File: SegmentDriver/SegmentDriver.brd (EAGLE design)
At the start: 175 x 175 mm, 221 parts, among them IC1 ATMEGA644A, IC2 PCA9555PW, IC3 4511D, K1 691313710002, K10 M02-MOLEX-104188-0210, K11 M02-MOLEX-104188-0210, K12 M02-MOLEX-104188-0210, K13 M02-MOLEX-104188-0210, K14 M02-MOLEX-104188-0210, K15 M02-MOLEX-104188-0210, K16 M02-MOLEX-104188-0210, K17 691210910004, K18 691210910004, K19 691210910004, K2 691313710002, K20 691210910004, K21 691210910004, K22 691210910004, K23 691210910004, K24 691210910004, K25 691210910004, K3 691322310002, K4 691322310002, K6 61200621621, K7 61201021621, K8 M02-MOLEX-104188-0210, K9 M02-MOLEX-104188-0210, Q1 MOSFET-NCHANNEL-FDMS5672, Q2 MOSFET-NCHANNEL-FDMS5672, Q3 MOSFET-NCHANNEL-FDMS5672, Q4 MOSFET-NCHANNEL-FDMS5672, Q5 MOSFET-NCHANNEL-FDMS5672, Q6 MOSFET-NCHANNEL-FDMS5672, Q7 MOSFET-NCHANNEL-FDMS5672, Q8 MOSFET-NCHANNEL-FDMS5672, Q9 MOSFET-NCHANNEL-FDMS5672, SW1 SPST_TACT-EVQQ2, U1 DS1307SO8-TIGHT, U10 FOD8321, U11 FOD8321, U15 DMP2215L-7, U16 DMP2215L-7, U3 FOD8321, U4 FOD8321, U5 FOD8321, U6 FOD8321, U7 FOD8321, U8 FOD8321, U9 FOD8321, X1 53261-03, X2 53261-03, X3 53261-03, X4 53261-03, X5 53261-03, X6 53261-03, Y2 32.768kHz

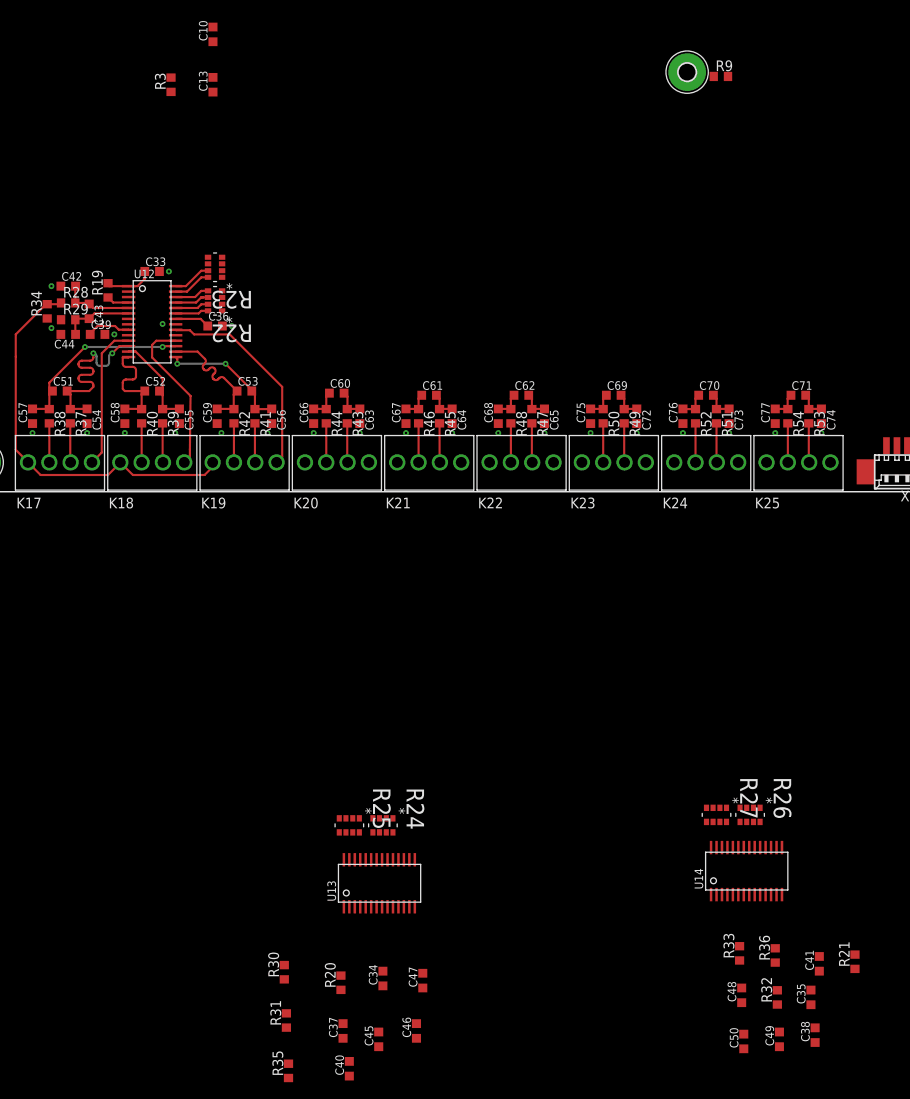
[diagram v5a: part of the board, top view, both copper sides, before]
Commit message: RTD AD layout, brd and sch remade consistent
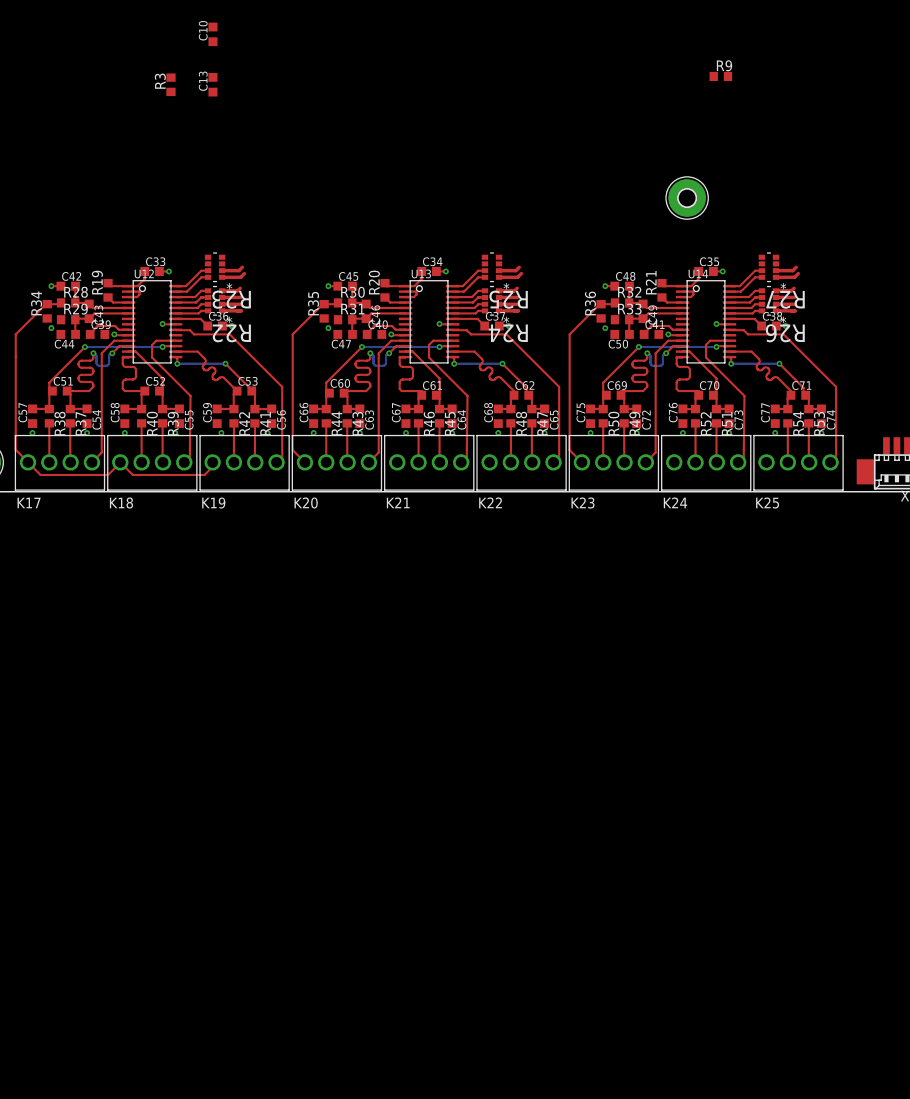
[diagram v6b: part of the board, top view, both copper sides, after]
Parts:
- moved R35 90.6 mm to (44.2, 21.5)
- moved C45 89.8 mm to (46.8, 24.5), turned to 0 degrees
- moved C49 88.3 mm to (82.2, 21.5), turned to 270 degrees
- moved C40 87.6 mm to (50.2, 18.8), turned to 0 degrees
- moved C35 87.4 mm to (89.8, 26.2), turned to 0 degrees
- moved C46 86.0 mm to (49.2, 21.5), turned to 270 degrees
- moved C37 85.9 mm to (64.2, 19.8), turned to 0 degrees
- moved C48 85.7 mm to (79.8, 24.5), turned to 0 degrees
- moved C50 85.5 mm to (79.8, 18.8), turned to 180 degrees
- moved R32 84.8 mm to (79.8, 22.5), turned to 0 degrees
- moved C38 84.7 mm to (97.2, 19.8), turned to 0 degrees
- moved C34 84.4 mm to (56.8, 26.2), turned to 0 degrees
- moved R31 83.8 mm to (46.8, 20.5), turned to 0 degrees
- moved R21 83.2 mm to (84.5, 24.0)
- moved R20 82.7 mm to (51.5, 24.0)
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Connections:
- net AD1_!CS renamed !CS!_AD1
- net AD1_!DRDY renamed !DRDY!_AD1
- net AD1_!RESET renamed !RESET!_AD1
- net AD1_BIASP renamed BIASP_AD1
- net AD1_IEXC1 renamed IEXC1_AD1
- net AD1_REFN0 renamed REFN0_AD1
- net AD1_REFP0 renamed REFP0_AD1
- net AD1_START renamed START_AD1
- net AD2_!CS renamed !CS!_AD2
- net AD2_!DRDY renamed !DRDY!_AD2
- net AD2_!RESET renamed !RESET!_AD2
- net AD2_IEXC1 renamed IEXC1_AD2
- net AD2_REFN0 renamed REFN0_AD2
- net AD2_REFP0 renamed REFP0_AD2
- net AD2_START renamed START_AD2
- net AD3_!CS renamed !CS!_AD3
- net AD3_!DRDY renamed !DRDY!_AD3
- net AD3_!RESET renamed !RESET!_AD3
- net AD3_IEXC1 renamed IEXC1_AD3
- net AD3_REFN0 renamed REFN0_AD3
- net AD3_REFP0 renamed REFP0_AD3
- net AD3_START renamed START_AD3
- net N$30 renamed 9_AD1
- net N$41 renamed 9_AD2
- net N$53 renamed 9_AD3
- net N$54 renamed 28_AD1
- net N$55 renamed 27_AD1
- net N$56 renamed 26_AD1
- net N$57 renamed 25_AD1
- net N$58 renamed 24_AD1
- net N$59 renamed 23_AD1
- net N$65 renamed 23_AD2
- net N$66 renamed 25_AD2
- net N$67 renamed 24_AD2
- net N$68 renamed 27_AD2
- net N$69 renamed 26_AD2
- net N$70 renamed 28_AD2
- net N$71 renamed 23_AD3
- net N$72 renamed 25_AD3
- net N$73 renamed 24_AD3
- net N$74 renamed 27_AD3
- net N$75 renamed 26_AD3
- net N$76 renamed 28_AD3
- removed net AD2_BIASP: K20.1, K21.1, K22.1, R30.1, R32.1, R35.2, R36.2
- removed net AD3_BIASP: K23.1, K24.1, K25.1
- new net BIASP_AD2: K20.1, K21.1, K22.1, R30.1, R35.2
- new net BIASP_AD3: K23.1, K24.1, K25.1, R32.1, R36.2
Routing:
- net GND: track 29.2 -> 58.8 mm, vias 8 -> 20
- net IEXC1_AD3: track 0.00 -> 24.8 mm
- net IEXC1_AD2: track 0.00 -> 24.8 mm
- net BIASP_AD3: track 0.00 -> 22.8 mm
- net BIASP_AD2: track 0.00 -> 22.8 mm
- net AD3_AIN1: track 3.32 -> 23.1 mm, vias 0 -> 2
- net AD2_AIN1: track 3.55 -> 23.1 mm, vias 0 -> 2
- net AD3_AIN3: track 0.00 -> 19.2 mm
- net AD2_AIN3: track 0.00 -> 19.2 mm
- net AD3_AIN2: track 3.32 -> 22.0 mm, vias 0 -> 2
- net AD2_AIN2: track 3.57 -> 22.0 mm, vias 0 -> 2
- net AD3_AIN0: track 0.00 -> 17.3 mm
- net AD2_AIN0: track 0.00 -> 17.3 mm
- net AD2_AIN7: track 3.32 -> 15.2 mm
- net AD3_AIN7: track 3.30 -> 15.2 mm
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
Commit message: added power rails
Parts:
- removed SW1: SPST_TACT-EVQQ2, adafruit:EVQ-Q2
- added C81, C84: 4.7uF, rcl:C0603K
- added C82, C83, C85: 4.7uF, rcl:C0805K
- added R62, R63, R64, R65, R66, R67, R68, R69, R70: 100k, rcl:R0603
- added SW2: (no value), simbits:434153017835
- added U18: 7808, simbits:D2PACK/A
- added U19: ADP3333ARM-5, simbits:MSOP-8
- added U20: 7805, simbits:D2PACK/A
- moved C10 204.4 mm to (235.0, 42.5)
- moved C11 204.4 mm to (235.0, 48.5)
- moved C12 204.4 mm to (235.0, 53.5)
- moved C13 204.4 mm to (235.0, 36.5)
- moved C6 204.4 mm to (250.5, 61.5)
- moved C7 204.4 mm to (255.0, 49.0)
- moved C8 204.4 mm to (255.0, 55.0)
- moved C9 204.4 mm to (255.0, 61.0)
- moved R1 204.4 mm to (244.0, 65.5)
- moved R2 204.4 mm to (238.5, 63.0)
- moved R3 204.4 mm to (230.0, 36.5)
- moved R4 204.4 mm to (245.0, 62.0)
- moved R5 204.4 mm to (245.0, 50.0)
- moved R6 204.4 mm to (245.0, 56.0)
- moved R7 204.4 mm to (230.0, 56.5)
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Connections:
- removed net +12V: C15.1, C16.1, C17.1, C18.1, C19.1, C2.1, C20.1, C21.1, C22.1, C23.1, C4.1, C6.2, K3.1, K4.2, R2.2, U10.6, U11.6, U3.6, U4.6, U5.6, U6.6, U7.6, U8.6, U9.6
- removed net AVDD: C36.1, C37.1, C38.1, U12.22, U13.22, U14.22
- removed net CS_ADS1248_1: IC1.35
- removed net CS_ADS1248_2: IC1.36
- removed net CS_ADS1248_3: IC1.37
- removed net DVDD: C33.1, C34.1, C35.1, R19.2, R20.2, R21.2, U12.1, U13.1, U14.1
- removed net N$83: IC2.7, R58.4
- removed net N$84: IC2.8, R59.1
- removed net N$85: IC2.9, R59.2
- removed net N$86: IC2.10, R59.3
- removed net N$87: IC2.11, R59.4
- new net !ADCSUP_SD: U19.7
- new net +15V: C15.1, C16.1, C17.1, C18.1, C19.1, C2.1, C20.1, C21.1, C22.1, C23.1, C4.1, C6.2, K3.1, K4.2, R2.2, U10.6, U11.6, U18.1, U3.6, U4.6, U5.6, U6.6, U7.6, U8.6, U9.6
- new net +8V: C82.2, C83.2, C85.2, U18.3, U19.2, U20.1
- new net ADC_5V: C33.1, C34.1, C35.1, C36.1, C37.1, C38.1, C81.2, R19.2, R20.2, R21.2, R62.2, R63.2, R64.2, R65.2, R66.2, R67.2, U12.1, U12.22, U13.1, U13.22, U14.1, U14.22, U19.1
- new net N$30: IC2.4, R58.4
- new net N$41: IC2.8, R59.4
- new net N$53: IC2.9, R59.3
- new net N$54: IC2.10, R59.2
- new net N$55: IC2.11, R59.1
- new net N$58: IC1.31
- net !CS!_AD1: now also IC1.37, R63.1
- net !CS!_AD2: now also IC1.36, R64.1
- net !CS!_AD3: now also IC1.35, R66.1
- net !DRDY!_AD1: now also IC1.40, R62.1
- net !DRDY!_AD2: now also IC1.41, R65.1
- net !DRDY!_AD3: now also IC1.42, R67.1
- net !RESET: now also SW2.1, SW2.3; no longer SW1.A, SW1.A'
- net +5V: now also C84.2, U20.3
- net 5V: now also R69.2, R70.2
- net GND: now also C81.1, C82.1, C83.1, C84.1, C85.1, R68.1, SW2.2, SW2.4, U18.2, U18.TAB, U19.3, U19.4, U19.5, U19.6, U19.8, U20.2, U20.TAB; no longer SW1.B, SW1.B'
- net GPIO1: now also R58.5; no longer R58.8
- net GPIO2: now also R58.6; no longer R58.7
- net GPIO3: now also R58.7; no longer R58.6
- net GPIO4: now also R58.8; no longer R58.5
- net GPIO5: now also R59.5; no longer R59.8
- net GPIO6: now also R59.6; no longer R59.7
- net GPIO7: now also R59.7; no longer R59.6
- net GPIO8: now also R59.8; no longer R59.5
- net LED1: now also IC1.14; no longer IC1.30
- net LED2: now also IC1.13; no longer IC1.31
- net MISO: now also R69.1
- net MOSI: now also R70.1
- net N$36: now also IC2.5, R58.3; no longer IC2.4, R58.1
- net N$37: now also IC2.6; no longer IC2.5
- net N$38: now also IC2.7, R58.1; no longer IC2.6, R58.3
- net SCK: now also R68.2
- net START_AD1: now also IC1.34
- net START_AD2: now also IC1.33
- net START_AD3: now also IC1.32
- net UART_DE: now also IC1.30; no longer IC1.32
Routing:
- net +15V: track 0.00 -> 30.6 mm
- net +12V: track 30.6 -> 0.00 mm
- net ADC_5V: track 0.00 -> 21.8 mm
- net DVDD: track 17.6 -> 0.00 mm
- net AVDD: track 12.5 -> 0.00 mm

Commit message: gpio connections
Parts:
- added JP1: (no value), SparkFun-Connectors:2X3
- added R71, R72, R73: 100k, rcl:R0603
- added R74, R75: 10k, rcl:R0603
- moved LED7 39.3 mm to (139.0, 18.0)
- moved U18 4.00 mm to (45.0, 74.0)
- moved U20 3.00 mm to (62.0, 74.0)
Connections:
- net GPIO1 renamed GPIO0.0
- net GPIO2 renamed GPIO0.1
- net GPIO3 renamed GPIO0.2
- net GPIO4 renamed GPIO0.3
- net GPIO5 renamed GPIO0.4
- net GPIO6 renamed GPIO0.5
- removed net GPIO7: R59.7
- removed net GPIO8: R59.8
- removed net LED2: IC1.13, R8.1
- removed net N$64: U17.2
- new net GPIO0.6_OUT: K5.B4, R59.7
- new net GPIO0.7_OUT: K5.B7, R59.8
- new net GPIO1.6_IN: IC2.19, K5.A4, R74.1
- new net GPIO1.7_IN: IC2.20, K5.A7, R75.1
- new net N$56: IC1.13, JP1.5, R73.1
- new net N$57: IC1.14, JP1.3, R72.1
- new net N$59: IC1.43, R8.1
- net !ADCSUP_SD: now also IC1.31
- net +5V: now also R74.2, R75.2
- net 5V: now also R71.2, R72.2, R73.2
- net GND: now also JP1.2, JP1.4, JP1.6, K5.A5, K5.A6, K5.A8, K5.B5, K5.B6, K5.B8, U17.2
- net LED1: now also IC1.44; no longer IC1.14
- net N$58: now also IC1.15, JP1.1, R71.1; no longer IC1.31
- net RS485+: now also K5.B2; no longer K5.B1
- net RS485-: now also K5.B1; no longer K5.B2
- net RTC_1HZ_CLK: now also K5.A3, K5.B3
